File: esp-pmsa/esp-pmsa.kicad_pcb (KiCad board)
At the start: 2 copper layers, 40 x 47.5 mm, 12 parts, among them M1 PMSA003, U1 WeMos_D1_mini_Labels, U2 BME68x, U3 OPT3001DNPT

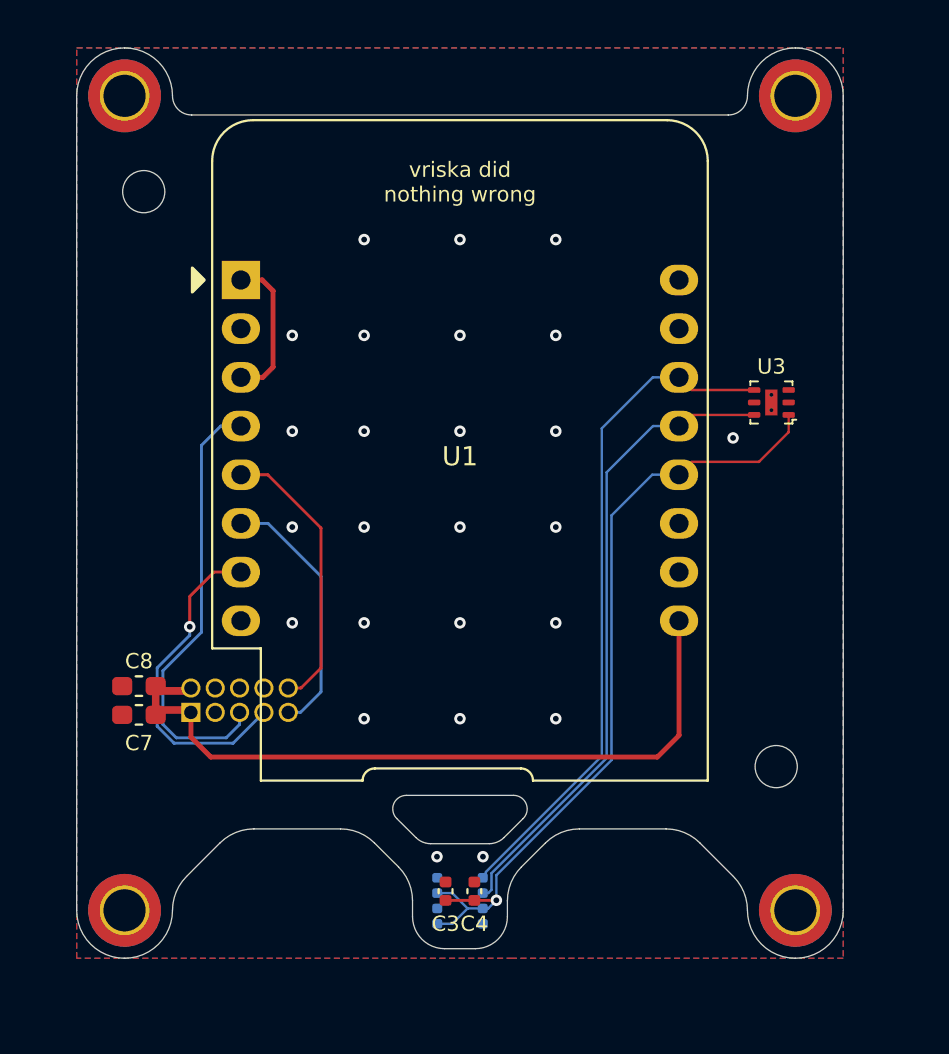
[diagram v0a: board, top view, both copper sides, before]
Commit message: switch to ESP-C3-F
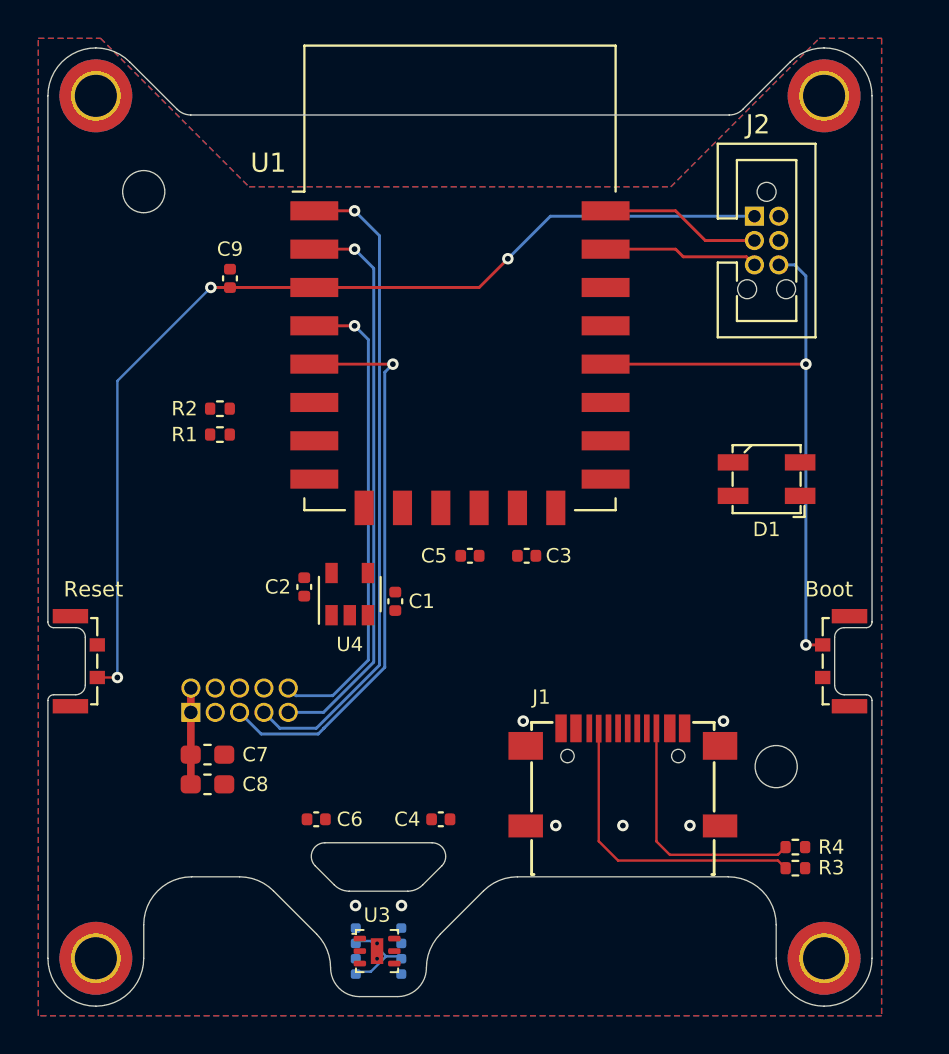
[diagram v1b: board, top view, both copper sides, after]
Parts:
- added C1: 10u, Capacitor_SMD:C_0402_1005Metric, F.Cu at (166.6, 103.9)
- added C2: 10u, Capacitor_SMD:C_0402_1005Metric, F.Cu at (161.9, 103.1)
- added C5: 1u, Capacitor_SMD:C_0402_1005Metric, F.Cu at (170.5, 101.5)
- added C6: 0.1u, Capacitor_SMD:C_0402_1005Metric, F.Cu at (162.5, 115.2)
- added C9: 0.1u, Capacitor_SMD:C_0402_1005Metric, F.Cu at (158.0, 87.0)
- added D1: APA104-12-3535, 21-SnapEDA-zip:LED_APA104-12-3535, F.Cu at (186.0, 97.5)
- added J1: USB_C_Receptacle_USB2.0_304S-ACP16, 41-EasyEDA-Edits:USB-C-SMD_TYPEC-304S-ACP16, F.Cu at (178.5, 113.0)
- added J2: ESP-PROG, 11-My-Edits:TC2030_IDCBox_2x03_P1.25mm_Vertical_3D, F.Cu at (186.0, 85.0)
- added R1: 4k7, Resistor_SMD:R_0402_1005Metric, F.Cu at (157.5, 95.2)
- added R2: 4k7, Resistor_SMD:R_0402_1005Metric, F.Cu at (157.5, 93.8)
- added R3: 5k1, Resistor_SMD:R_0402_1005Metric, F.Cu at (187.5, 117.8)
- added R4: 5k1, Resistor_SMD:R_0402_1005Metric, F.Cu at (187.5, 116.7)
- added SW1: Reset, 41-EasyEDA-Edits:SW-SMD_SKSLLAE010-3D, F.Cu at (150.4, 107.0)
- added SW2: Boot, 41-EasyEDA-Edits:SW-SMD_SKSLLAE010-3D, F.Cu at (189.6, 107.0)
- added U4: XC6220B331MR, Package_TO_SOT_SMD:SOT-23-5, F.Cu at (164.2, 103.5)
- C3: value 1uF -> 1u
- C4: value 100nF -> 0.1u
- C7, C8: value 10uF -> 10u
- U1: value WeMos_D1_mini_Labels -> ESP32-C3F; footprint 11-My-Edits:WEMOS_D1_mini -> 11-My-Edits:ESP-12H
- moved U3 35.3 mm to (165.7, 122.1), turned to 0 degrees
- moved C3 18.0 mm to (173.5, 101.5), turned to 0 degrees
- moved U1 9.00 mm to (170.0, 87.0)
- moved C8 6.25 mm to (156.8, 113.4), turned to 0 degrees
- moved U2 5.00 mm to (165.8, 122.1)
- moved C4 4.14 mm to (169.0, 115.2), turned to 180 degrees
- moved C7 4.13 mm to (156.8, 111.9), turned to 0 degrees
- moved H2 2.92 mm to (189.0, 122.5)
- moved H4 2.92 mm to (151.0, 122.5)
- moved H1 1.50 mm to (151.0, 77.5)
- moved H3 1.50 mm to (189.0, 77.5)
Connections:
- C3 pad 1: /VCC_SENS -> /VCC_BME
- C4 pad 1: GND -> /VCC_BME
- C4 pad 2: /VCC_SENS -> GND
- M1 pad 8: Net-(M1-Pad8) -> Net-(M1-Pad6)
- U1 pad 1: /~WAKE -> /PMS_RX
- U1 pad 10: GND -> Net-(U1-Pad10)
- U1 pad 11: Net-(U1-Pad11) -> Net-(U1-Pad10)
- U1 pad 12: /VCC_SENS -> /VCC_ALS
- U1 pad 13: /SDA -> /VCC_BME
- U1 pad 14: /SCL -> Net-(U1-Pad10)
- U1 pad 15: /U0RXD -> GND
- U1 pad 16: /U0TXD -> (no net)
- U1 pad 2: Net-(U1-Pad2) -> /PMS_TX
- U1 pad 3: /~WAKE -> /~RST
- U1 pad 4: /~PMS_RST -> /~PMS_SET
- U1 pad 5: /~PMS_SET -> /~PMS_RST
- U1 pad 6: /PMS_TX -> /SDA
- U1 pad 7: /PMS_RX -> /SCL
- U1 pad 9: +5V -> Net-(U1-Pad10)
- U2 pad 2: /VCC_SENS -> /VCC_BME
- U2 pad 6: /VCC_SENS -> /VCC_BME
- U2 pad 8: /VCC_SENS -> /VCC_BME
- U3 pad 1: /VCC_SENS -> /VCC_ALS
- U3 pad 5: Net-(U3-Pad5) -> (no net)
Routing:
- net /~RST: track 0.00 -> 53.6 mm, vias 0 -> 3
- net /VCC_SENS: track 42.8 -> 0.00 mm, vias 1 -> 0
- net /SCL: track 35.5 -> 0.00 mm
- net +5V: track 39.4 -> 5.03 mm
- net /SDA: track 33.8 -> 0.00 mm
- net /~BOOT: track 0.00 -> 32.2 mm, vias 0 -> 2
- net /PMS_RX: track 17.0 -> 34.1 mm
- net Net-(J1-PadA5): track 0.00 -> 16.2 mm
- net /PMS_TX: track 13.5 -> 29.6 mm, vias 0 -> 1
- net Net-(J1-PadB5): track 0.00 -> 13.1 mm
- net /~PMS_SET: track 14.8 -> 25.0 mm, vias 0 -> 1
- net /U0TXD: track 0.00 -> 8.41 mm
- net /U0RXD: track 0.00 -> 8.10 mm
- net /~WAKE: track 7.79 -> 0.00 mm
- net /~PMS_RST: track 23.1 -> 29.6 mm, vias 0 -> 1
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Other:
- board size 40 x 47.5 mm -> 43 x 50 mm
- board text added: "Boot"
- board text added: "Reset"
- board text removed: "vriska did nothing wrong"

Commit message: okeydokey!
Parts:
- added LOGO1: neggles logo, 10-My-Footprints:neggle-logo-0.12, F.Cu at (181.5, 103.5)
- U2: moved to F.Cu
- U4: value XC6220B331MR -> XC6210B332MR
- moved U3 8.77 mm to (167.2, 113.5), turned to 180 degrees
- moved C6 7.17 mm to (169.5, 113.7), turned to 90 degrees
- moved C4 4.60 mm to (170.8, 119.5), turned to 45 degrees
- moved C1 4.37 mm to (162.3, 104.5)
- moved R1 3.04 mm to (160.5, 95.5)
- moved R2 3.04 mm to (160.5, 93.5)
- moved C9 2.54 mm to (160.5, 87.5), turned to 0 degrees
- moved U2 1.51 mm to (167.2, 122.0)
- moved C3 1.50 mm to (175.0, 101.5)
- moved C5 1.50 mm to (172.0, 101.5)
- moved C7 1.50 mm to (158.3, 111.9)
- moved C8 1.50 mm to (158.3, 113.4)
- moved D1 1.50 mm to (187.5, 97.5)
- moved H1 1.50 mm to (152.5, 77.5)
- moved H2 1.50 mm to (190.5, 122.5)
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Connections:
- SW1 pad MP: (no net) -> GND
- SW2 pad MP: (no net) -> GND
- U1 pad 10: Net-(U1-Pad10) -> (no net)
- U1 pad 11: Net-(U1-Pad10) -> (no net)
- U1 pad 14: Net-(U1-Pad10) -> (no net)
- U1 pad 9: Net-(U1-Pad10) -> (no net)
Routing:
- net +5V: track 5.03 -> 55.6 mm
- net /SDA: track 0.00 -> 41.0 mm, vias 0 -> 3
- net /SCL: track 0.00 -> 38.0 mm, vias 0 -> 2
- net /USB_D-: track 0.00 -> 29.4 mm, vias 0 -> 2
- net /USB_D+: track 0.00 -> 27.7 mm, vias 0 -> 2
- net /VCC_BME: track 4.63 -> 30.0 mm, vias 0 -> 2
- net /VCC_ALS: track 0.00 -> 20.5 mm, vias 0 -> 2
- net +3V3: track 0.00 -> 14.5 mm
- net /RGB: track 0.00 -> 7.94 mm
- net GND: track 0.00 -> 3.52 mm, vias 7 -> 58
- net /~RST: track 53.6 -> 51.8 mm
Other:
- net class USB_D: clearance 0.1524 -> 0.254
- net class VCC: trace_width 0.2 -> 0.1524
- net class VIN: clearance 0.254 -> 0.1524; trace_width 0.4 -> 0.1524
- board text added: "IO0/~BOOT"
- board text added: "JLCJLCJLCJLC"
- board text added: "neg2led.github.io/esp-pmsa"
- board text added: "v1.0"
- board text removed: "Boot"

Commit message: layout tweaks
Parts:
- moved C4 3.91 mm to (172.5, 116.0), turned to 90 degrees
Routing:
- net /VCC_ALS: track 20.5 -> 19.8 mm

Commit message: okay that's better
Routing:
- net /VCC_BME: track 30.0 -> 31.0 mm
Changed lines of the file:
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@@
     (thickness 1.6002)
     (drawings 51)
-    (tracks 263)
+    (tracks 264)
     (zones 0)
     (modules 28)
@@
     (add_net /VCC_ALS)
     (add_net /VCC_BME)
+    (add_net /VPP)
     (add_net /~BOOT)
     (add_net /~PMS_RST)
@@
     (add_net /~RST)
     (add_net GND)
+    (add_net "Net-(D1-Pad1)")
     (add_net "Net-(J1-PadA5)")
+    (add_net "Net-(J1-PadA8)")
     (add_net "Net-(J1-PadB5)")
+    (add_net "Net-(J1-PadB8)")
     (add_net "Net-(M1-Pad6)")
+    (add_net "Net-(U1-Pad10)")
+    (add_net "Net-(U1-Pad11)")
+    (add_net "Net-(U1-Pad14)")
+    (add_net "Net-(U1-Pad16)")
+    (add_net "Net-(U1-Pad9)")
+    (add_net "Net-(U3-Pad5)")
+    (add_net "Net-(U4-Pad4)")
   )
   (net_class USB_D ""
@@
   (segment (start 169.3 121.2) (end 169.3 120.7) (width 0.1524) (layer Front) (net 9))
   (segment (start 168.4375 121.6) (end 168.9 121.6) (width 0.1524) (layer Front) (net 9))
+  (segment (start 172.5 117.5) (end 172.5 116.48) (width 0.127) (layer Front) (net 9))
   (via (at 172.5 102.5) (size 0.6) (drill 0.3) (layers Front Back) (net 10))
   (segment (start 172.5 102.5) (end 172.5 101.5) (width 0.1524) (layer Front) (net 10))

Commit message: update for kicad 6
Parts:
- J1: value USB_C_Receptacle_USB2.0_304S-ACP16 -> USB-C
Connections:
- net /~BOOT renamed /~{BOOT}
- net /~PMS_RST renamed /~{PMS_RST}
- net /~PMS_SET renamed /~{PMS_SET}
- net /~RST renamed /~{RST}
- M1 pad 6: Net-(M1-Pad6) -> (no net)
- M1 pad 8: Net-(M1-Pad6) -> (no net)
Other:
- net class Default removed
- net class USB_D removed
- net class VCC removed
- net class VIN removed
- board text added: "IO0/~{BOOT}"
- board text removed: "IO0/~BOOT"
